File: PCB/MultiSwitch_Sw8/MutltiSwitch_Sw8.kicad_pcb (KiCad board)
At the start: 2 copper layers, 38.7 x 32.4 mm, 33 parts, among them IC1 ATTINY84-P, IC2 ULN2803, P1 +V=VRx / +V<VRx, P10 OUTPUT_1X8_GND, P2 XANY_INPUT, P3 SERVO, P4 DIODE, P5 OUTPUT_1X8, P6 VExt, P7 OUTPUT_1X8_ALIM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

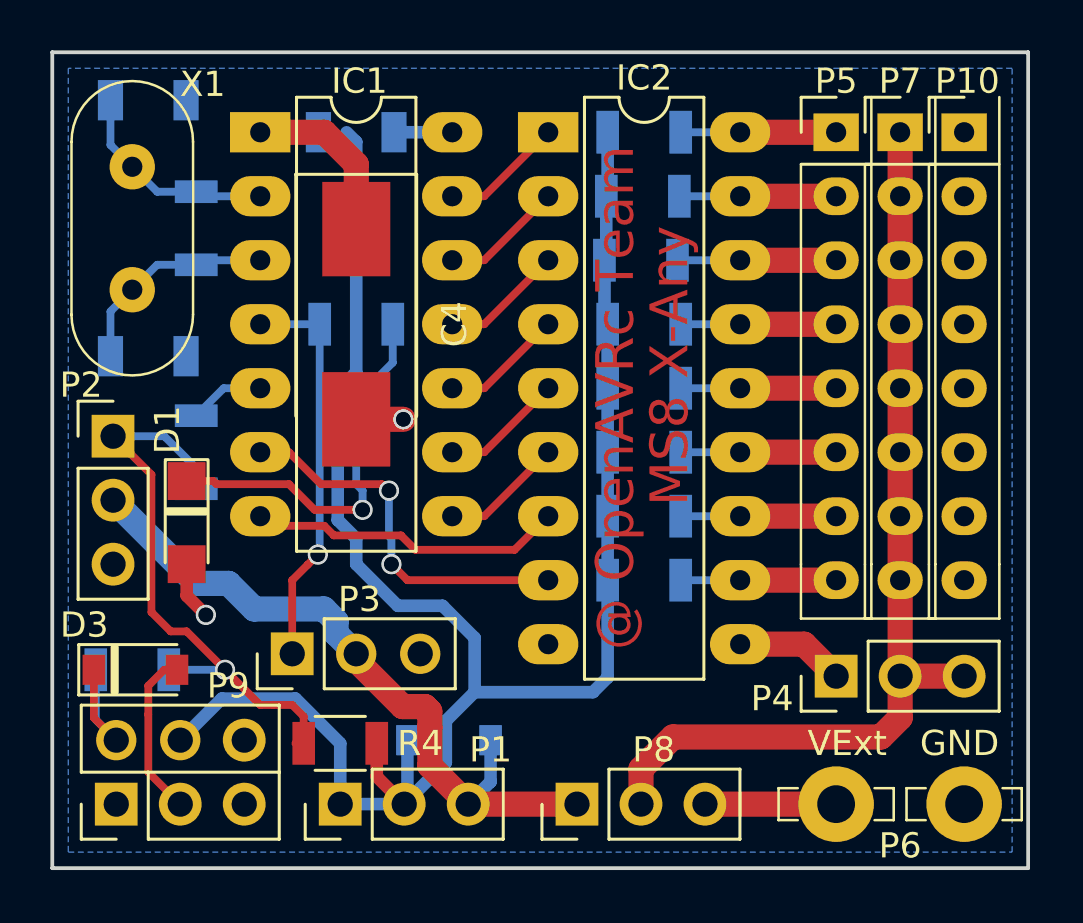
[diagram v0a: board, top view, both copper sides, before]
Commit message: Inverted diodes corrections
-Update pcb and silkscreen .
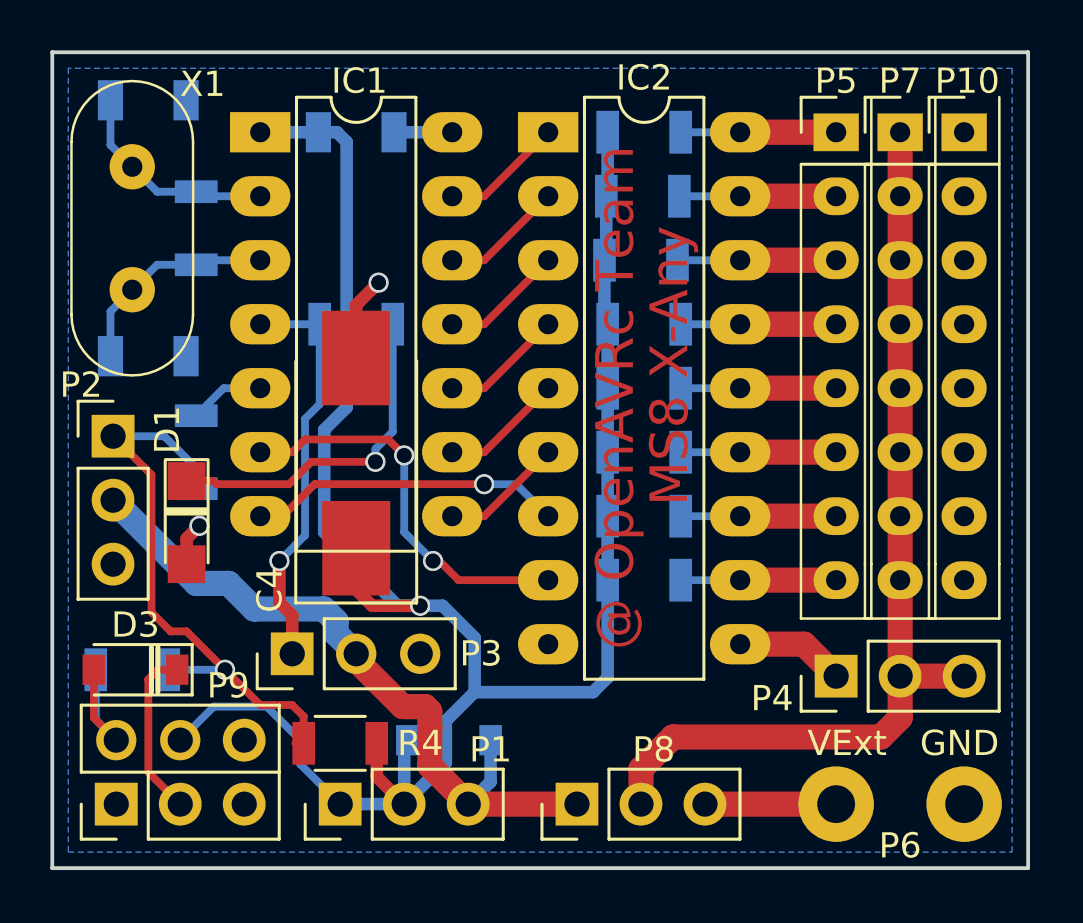
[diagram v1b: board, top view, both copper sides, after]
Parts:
- C4: value 200uF -> 220uF
- D1: footprint LED_1206 -> mylib:LED_1206
- D2, D3: footprint D_SOD-123 -> Diode_SMD:D_SOD-123
- P6: footprint Faston_V-5_08 -> mylib:Faston_V-5_08
- R2: value 330 -> 2,7K
- X1: footprint HC-39 -> mylib:HC-39
- moved C4 5.11 mm to (145.4, 104.2), turned to 90 degrees
- turned D2 to 0 degrees
- turned D3 to 180 degrees
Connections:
- D2 pad 1: +VRx -> +5V
- D2 pad 2: +5V -> +VRx
- P9 pad 2: Net-(D3-Pad1) -> Net-(D3-Pad2)
- P9 pad 3: Net-(D3-Pad2) -> Net-(D3-Pad1)
- R3 pad 1: Net-(D3-Pad1) -> Net-(D3-Pad2)
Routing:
- net +5V: track 86.3 -> 83.9 mm, vias 0 -> 1
- net Net-(D1-Pad1): track 15.8 -> 13.9 mm
- net Net-(IC1-Pad6): track 15.2 -> 15.7 mm
- net Net-(IC1-Pad7): vias 0 -> 1
